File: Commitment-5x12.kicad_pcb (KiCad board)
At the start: 2 copper layers, 234.4 x 118.4 mm, 97 parts, among them J1 Conn_01x13, J2 Conn_01x13, J3 Conn_01x03, J4 Conn_01x04, J5 Conn_01x04, SW1 OS102011MS2QN1, SW2 RotaryEncoder, SW3 SW_SPST

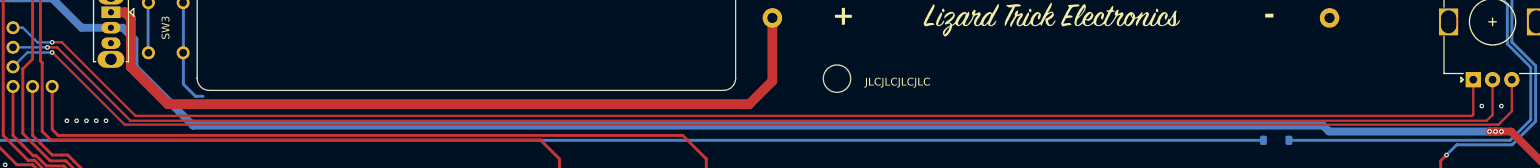
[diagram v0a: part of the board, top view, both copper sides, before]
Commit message: Disconnected encoder C from microcontroller and connected it to ground
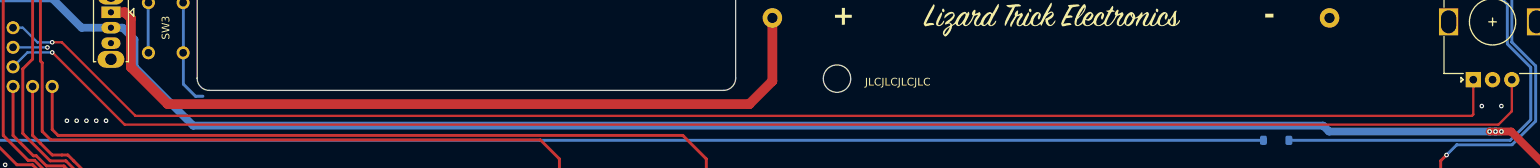
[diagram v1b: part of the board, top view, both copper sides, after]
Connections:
- J3 pad 2: Net-(J3-Pin_2) -> unconnected-(J3-Pin_2-Pad2)
- SW2 pad C: Net-(J3-Pin_2) -> GND
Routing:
- net Net-(J3-Pin_2): track 200.7 -> 0.00 mm, vias 1 -> 0
- net unconnected-(J3-Pin_2-Pad2): track 0.00 -> 4.47 mm, vias 0 -> 1
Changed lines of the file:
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@@
 	(net 87 "unconnected-(H8-Pad1)")
 	(net 88 "Net-(J2-Pin_10)")
-	(net 89 "Net-(J3-Pin_2)")
+	(net 89 "unconnected-(J3-Pin_2-Pad2)")
 	(net 90 "Net-(J3-Pin_1)")
 	(net 91 "Net-(J3-Pin_3)")
@@
 			(layers "*.Cu" "*.Mask")
 			(remove_unused_layers no)
-			(net 89 "Net-(J3-Pin_2)")
+			(net 2 "GND")
 			(pinfunction "C")
 			(pintype "passive")
@@
 			(layers "*.Cu" "*.Mask")
 			(remove_unused_layers no)
-			(net 89 "Net-(J3-Pin_2)")
+			(net 89 "unconnected-(J3-Pin_2-Pad2)")
 			(pinfunction "Pin_2")
 			(pintype "passive")
@@
 		(net 88)
 	)
-	(segment
-		(start 61.6124 39.3874)
-		(end 71.12 48.895)
-		(width 0.3048)
-		(layer "F.Cu")
-		(net 89)
-	)
-	(segment
-		(start 247.777 48.133)
-		(end 247.777 43.568)
-		(width 0.3048)
-		(layer "F.Cu")
-		(net 89)
-	)
-	(segment
-		(start 247.015 48.895)
-		(end 247.777 48.133)
-		(width 0.3048)
-		(layer "F.Cu")
-		(net 89)
-	)
-	(segment
-		(start 60.3424 39.3874)
-		(end 61.6124 39.3874)
-		(width 0.3048)
-		(layer "F.Cu")
-		(net 89)
-	)
-	(segment
-		(start 71.12 48.895)
-		(end 247.015 48.895)
-		(width 0.3048)
-		(layer "F.Cu")
-		(net 89)
-	)
 	(via

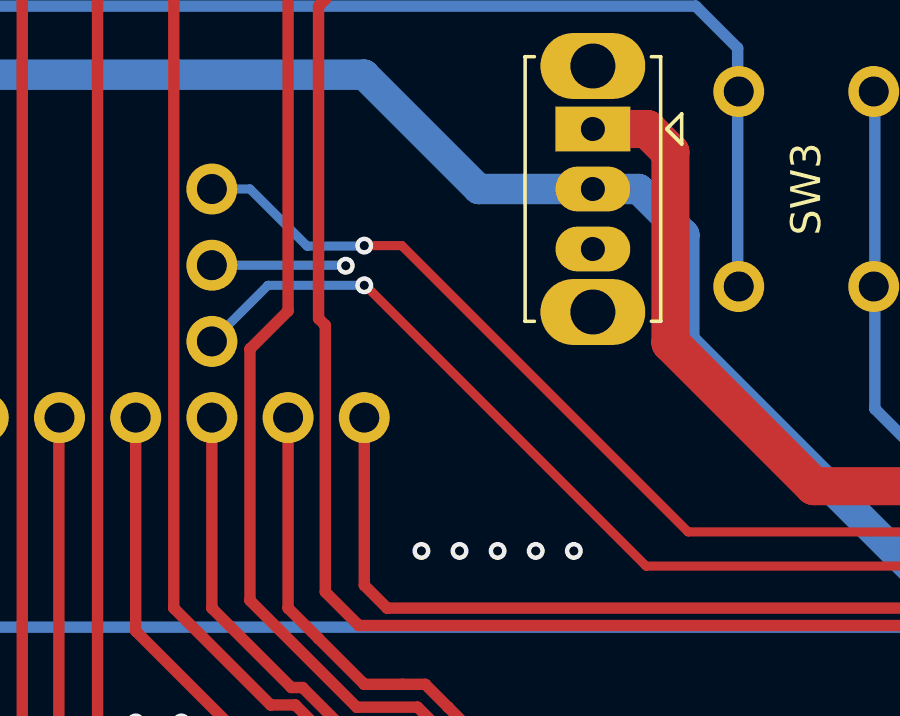
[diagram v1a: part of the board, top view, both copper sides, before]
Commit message: Minor routing adjustment
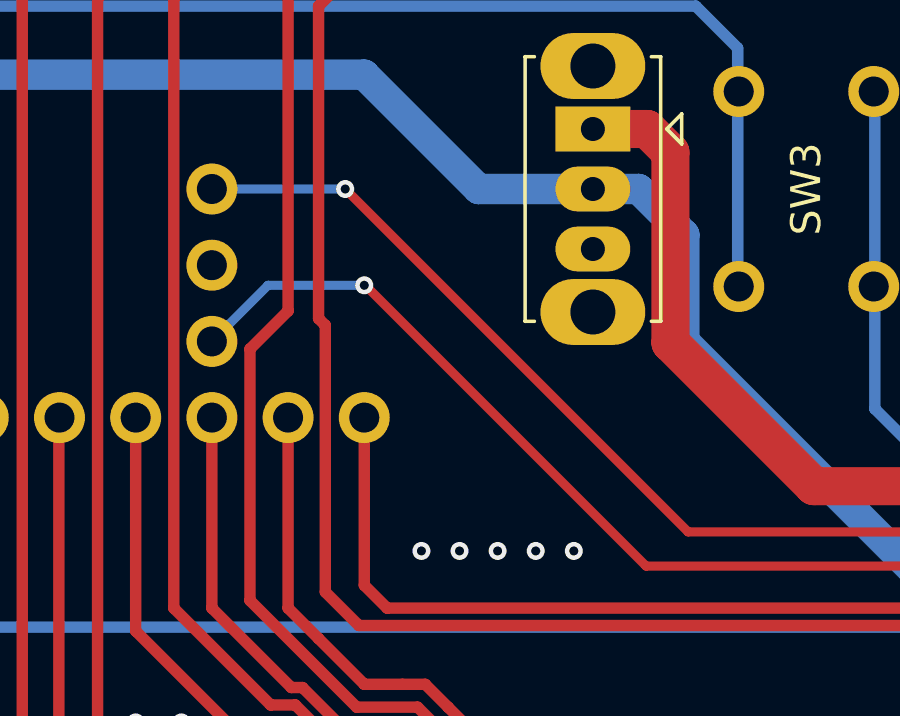
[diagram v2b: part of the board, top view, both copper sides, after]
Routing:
- net unconnected-(J3-Pin_2-Pad2): track 4.47 -> 0.00 mm, vias 1 -> 0
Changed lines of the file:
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@@
 		(net 88)
 	)
-	(via
-		(at 60.3424 39.3874)
-		(size 0.6)
-		(drill 0.3)
-		(layers "F.Cu" "B.Cu")
-		(net 89)
-	)
 	(segment
-		(start 60.325 39.37)
-		(end 55.88 39.37)
-		(width 0.3048)
-		(layer "B.Cu")
-		(net 89)
-	)
-	(segment
-		(start 60.3424 39.3874)
-		(end 60.325 39.37)
-		(width 0.3048)
-		(layer "B.Cu")
-		(net 89)
-	)
-	(segment
-		(start 60.96 38.7176)
-		(end 62.2126 38.7176)
-		(width 0.3048)
-		(layer "F.Cu")
-		(net 90)
-	)
-	(segment
-		(start 245.277 48.093)
-		(end 245.277 43.568)
+		(start 71.755 48.26)
+		(end 245.11 48.26)
 		(width 0.3048)
 		(layer "F.Cu")
@@
 	)
 	(segment
-		(start 71.755 48.26)
-		(end 245.11 48.26)
+		(start 60.325 36.83)
+		(end 71.755 48.26)
 		(width 0.3048)
 		(layer "F.Cu")
@@
 	)
 	(segment
-		(start 62.2126 38.7176)
-		(end 71.755 48.26)
+		(start 245.277 48.093)
+		(end 245.277 43.568)
 		(width 0.3048)
 		(layer "F.Cu")
@@
 	)
 	(via
-		(at 60.96 38.7176)
+		(at 60.325 36.83)
 		(size 0.6)
 		(drill 0.3)
@@
 	)
 	(segment
-		(start 59.055 38.735)
-		(end 57.15 36.83)
-		(width 0.3048)
-		(layer "B.Cu")
-		(net 90)
-	)
-	(segment
-		(start 57.15 36.83)
+		(start 60.325 36.83)
 		(end 55.88 36.83)
 		(width 0.3048)
 		(layer "B.Cu")
-		(net 90)
-	)
-	(segment
-		(start 60.96 38.7176)
-		(end 60.9426 38.735)
-		(width 0.3048)
-		(layer "B.Cu")
-		(net 90)
-	)
-	(segment
-		(start 60.9426 38.735)
-		(end 59.055 38.735)
-		(width 0.3048)
-		(layer "B.Cu")
